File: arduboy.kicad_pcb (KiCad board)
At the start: 2 copper layers, 120 x 66 mm, 59 parts, among them J1 Conn_01x06_Pin, J2 Conn_01x01_Pin, J3 Conn_01x01_Pin, J4 Conn_01x01_Pin, J5 Conn_01x01_Pin, J6 Conn_01x01_Pin, J7 Conn_01x01_Pin, SW1 POWER, SW2 LEFT, SW3 UP, SW4 DOWN, SW5 RIGHT, SW6 A, SW7 B, SW8 RESET, U1 ATmega32U4-A, U2 USBLC6-2SC6, U3 MCP73831-2-OT, U4 W25Q128JVS, Y1 16MHz

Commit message: Add back silkscreen
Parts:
- removed R11: 86.6, arduboy:R_1210_3225Metric_Pad1.30x2.65mm_HandSolder with ref under the component
- added JP1: Jumper_2_Bridged, arduboy:Jumper for SMD 1210 bridged, F.Cu at (163.8, 58.7)
- added REF**: Battery chemistry, arduboy:Battery chemistry, B.Cu at (149.6, 77.3)
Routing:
- net SPEAKER +: track 55.6 -> 55.0 mm
- net CART CS: track 46.6 -> 46.1 mm
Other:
- board text added: "Yornn"
- board text added: "did a thing"

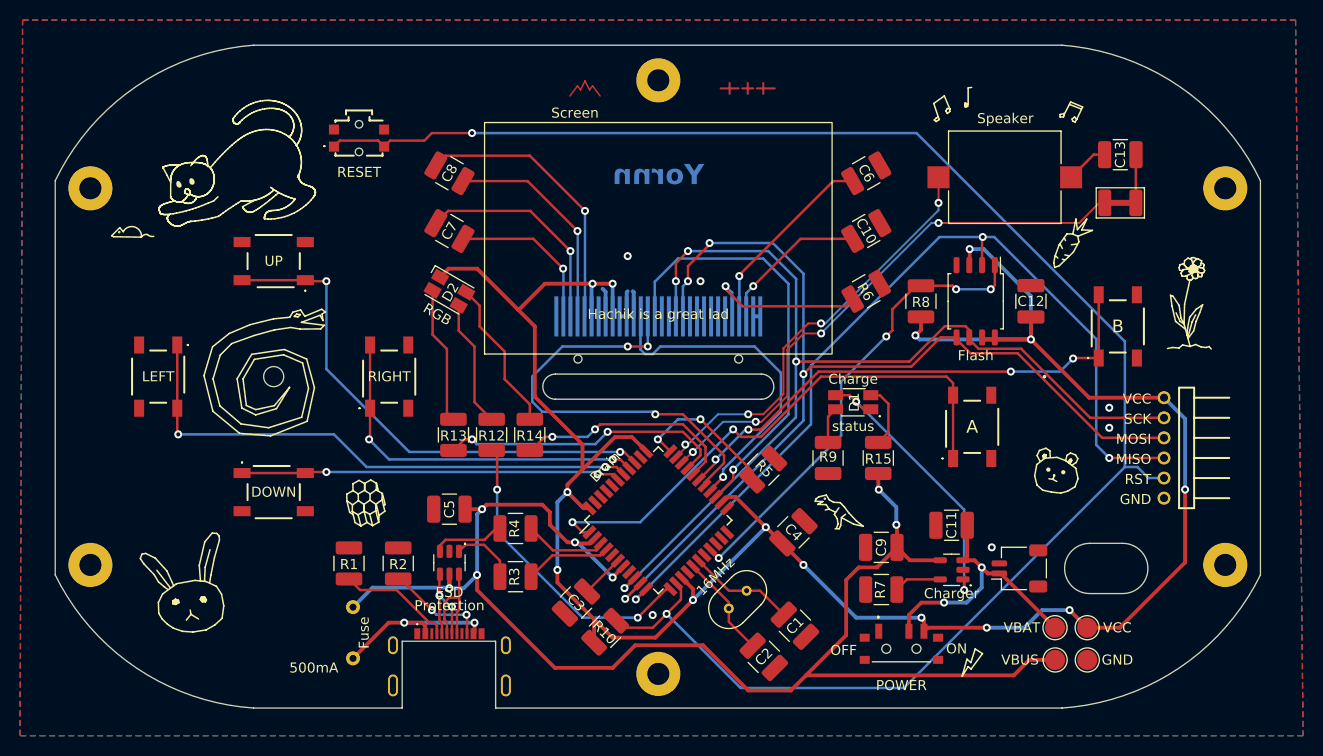
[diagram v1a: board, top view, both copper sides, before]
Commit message: Fix footprints to use 1210 according to selected components
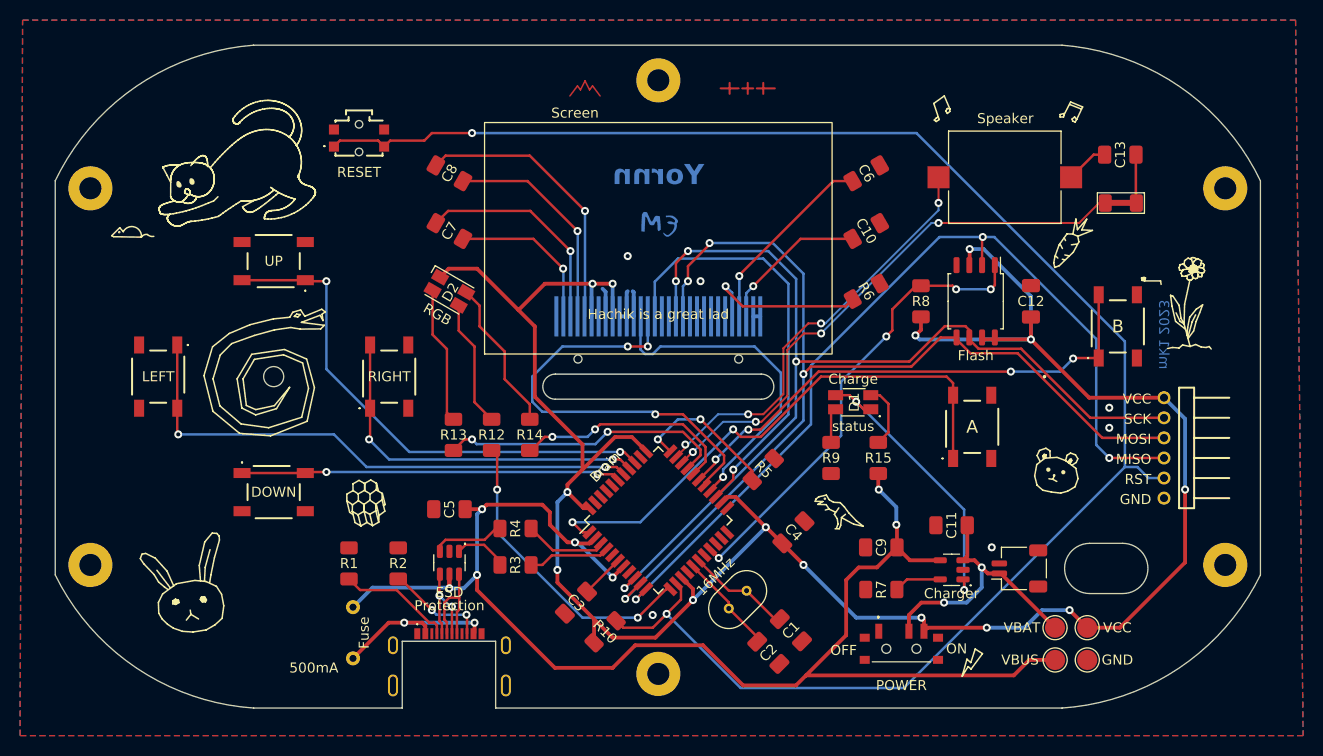
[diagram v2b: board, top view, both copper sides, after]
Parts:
- C1, C10, C11, C12, C13, C2, C3, C4, C5, C6, C7, C8, C9: footprint arduboy:C_1210_3225Metric_Pad1.33x2.70mm_HandSolder ref under the component -> arduboy:C_1206_3216Metric_Pad1.33x1.80mm_HandSolder ref under the component
- JP1: footprint arduboy:Jumper for SMD 1210 bridged -> arduboy:Jumper for SMD 1206 bridged
- R1, R10, R12, R13, R14, R15, R2, R3, R4, R5, R6, R7, R8, R9: footprint arduboy:R_1210_3225Metric_Pad1.30x2.65mm_HandSolder with ref under the component -> arduboy:R_1206_3216Metric_Pad1.30x1.75mm_HandSolder with ref under the component
- moved R3 1.17 mm to (103.6, 94.8)
- moved C1 0.60 mm to (131.0, 101.2)
- moved C2 0.60 mm to (128.8, 103.5)
- moved R9 0.30 mm to (135.0, 84.1)
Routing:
- net D+: track 6.59 -> 5.42 mm
- net RESET: track 171.8 -> 172.8 mm
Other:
- board text added: "and"
- board text added: "mk1 2023"
- board text removed: "did a thing"
